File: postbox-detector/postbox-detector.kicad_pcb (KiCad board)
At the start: 2 copper layers, 4 parts, among them U1 L86-M33, U3 LDS1117-3.3

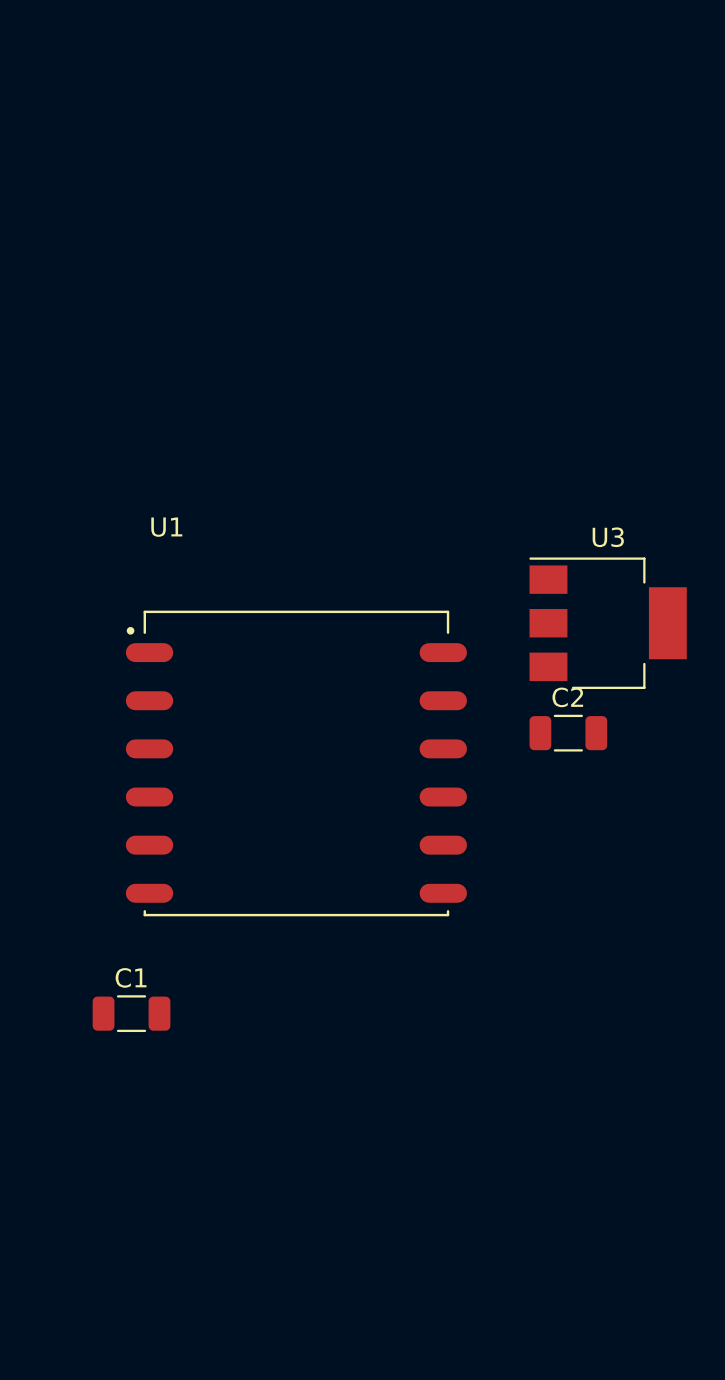
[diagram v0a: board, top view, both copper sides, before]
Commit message: crude test implementation and pcb layout
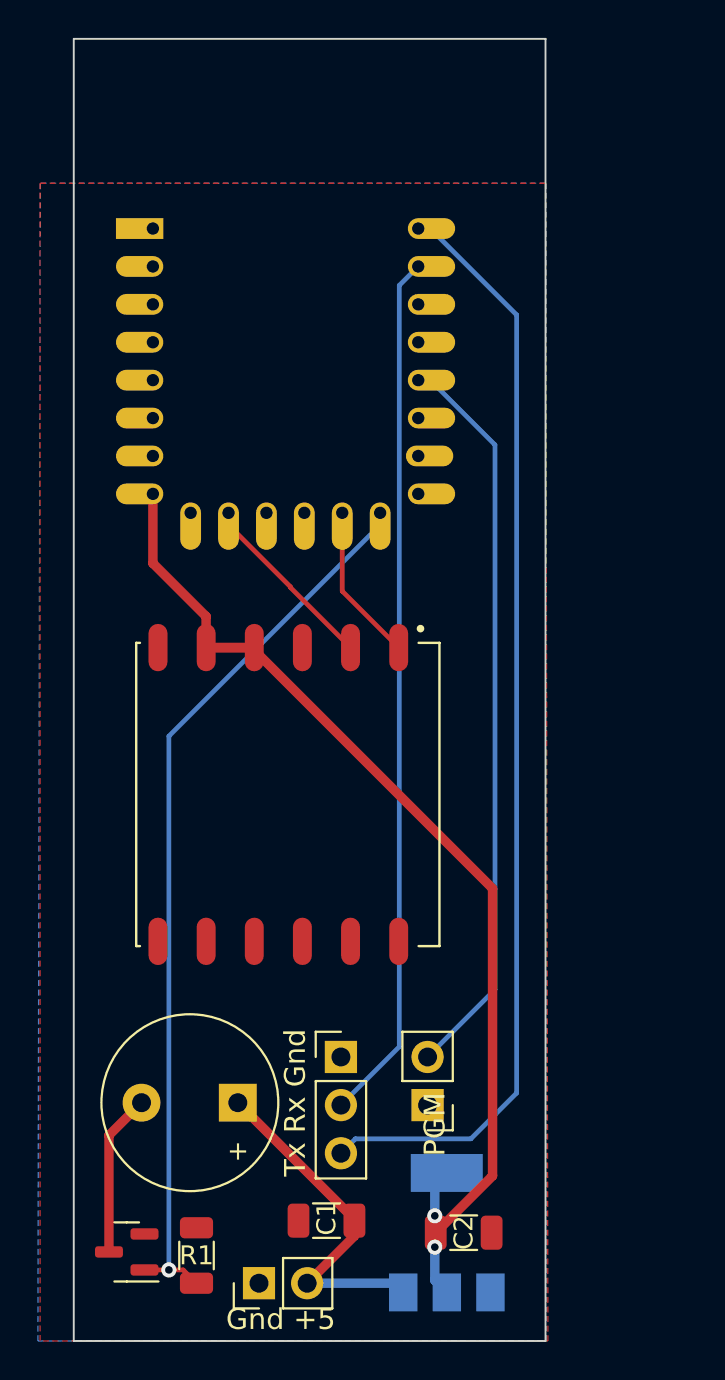
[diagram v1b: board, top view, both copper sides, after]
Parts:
- added BZ1: Buzzer, Custom:Buzzer_9.2x4.2_WST-0904T, F.Cu at (128.5, 80.1)
- added J1: UART, Connector_PinHeader_2.54mm:PinHeader_1x03_P2.54mm_Vertical, F.Cu at (134.0, 77.7)
- added J2: PGM, Connector_PinHeader_2.54mm:PinHeader_1x02_P2.54mm_Vertical, F.Cu at (138.6, 80.3)
- added J3: Power, Connector_PinHeader_2.54mm:PinHeader_1x02_P2.54mm_Vertical, F.Cu at (129.7, 89.7)
- added Q1: BSS138, Package_TO_SOT_SMD:SOT-23, F.Cu at (122.7, 88.0)
- added R1: 10K, Resistor_SMD:R_1206_3216Metric, F.Cu at (126.4, 88.2)
- added U2: ESP-12F, ESP8266:ESP-12E, F.Cu at (124.1, 34.0)
- U3: moved to B.Cu
- moved U3 33.3 mm to (139.6, 87.0), turned to 90 degrees
- moved C2 26.9 mm to (140.5, 87.0), turned to 180 degrees
- moved C1 15.0 mm to (133.2, 86.4)
- moved U1 1.48 mm to (130.7, 63.9), turned to -90 degrees
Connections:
- U1 pad 1: Net-(U1-Pad1) -> GpsRx
- U1 pad 2: Net-(U1-Pad2) -> GpsTx
- U1 pad 4: unconnected-(U1-Pad4) -> +3V3
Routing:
- net Tx: track 0.00 -> 58.7 mm
- net +3V3: track 0.00 -> 58.5 mm, vias 0 -> 2
- net Buzzer: track 0.00 -> 47.6 mm, vias 0 -> 1
- net Rx: track 0.00 -> 45.9 mm
- net Pgm: track 0.00 -> 39.2 mm
- net VCC: track 0.00 -> 18.4 mm
- net GpsTx: track 0.00 -> 9.78 mm
- net Net-(BZ1-Pad2): track 0.00 -> 8.59 mm
- net GpsRx: track 0.00 -> 8.34 mm
- added copper zone on B.Cu, net GND
- added copper zone on F.Cu, net GND
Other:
- board outline added: 24.9 x 68.7 mm
- board text added: "Gnd +5"
- board text added: "PGM"
- board text added: "Tx Rx Gnd"
